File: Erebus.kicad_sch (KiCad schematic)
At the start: 1 part, among them U1 STM32F303CBTx

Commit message: Setup Base Layout
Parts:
- added ENCODER1: EC11E, PCM_marbastlib-various:ROT_Alps_EC11E-Switch, symbol Device:RotaryEncoder_Switch
- added JP1, JP2: Jumper_2_Open, Connector_PinHeader_2.54mm:PinHeader_1x02_P2.54mm_Vertical, symbol Jumper:Jumper_2_Open
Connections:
- net ENCODER_A: now reaches U1.10 (PA0)
- net ENCODER_A: now also ENCODER1.A
- net ENCODER_B: now reaches U1.11 (PA1)
- net ENCODER_B: now also ENCODER1.B
- net GND: now reaches U1.23 (VSS), U1.35 (VSS), U1.47 (VSS)
- net GND: now also U1.8 (VSSA), ENCODER1.C, ENCODER1.S1, JP1.1 (A)
- net ENCODER_SW: now reaches U1.4 (PC15)
- net ENCODER_SW: now also ENCODER1.S2
- new net +3V3: JP2.1 (A)
- new net BOOT0: JP2.2 (B)
- new net ~{RESET}: JP1.2 (B)
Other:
- note added: "Keys"
- note added: "MCU Boot Select Jumpers"
- note added: "Rotary Encoder"
- moved on the sheet: U1

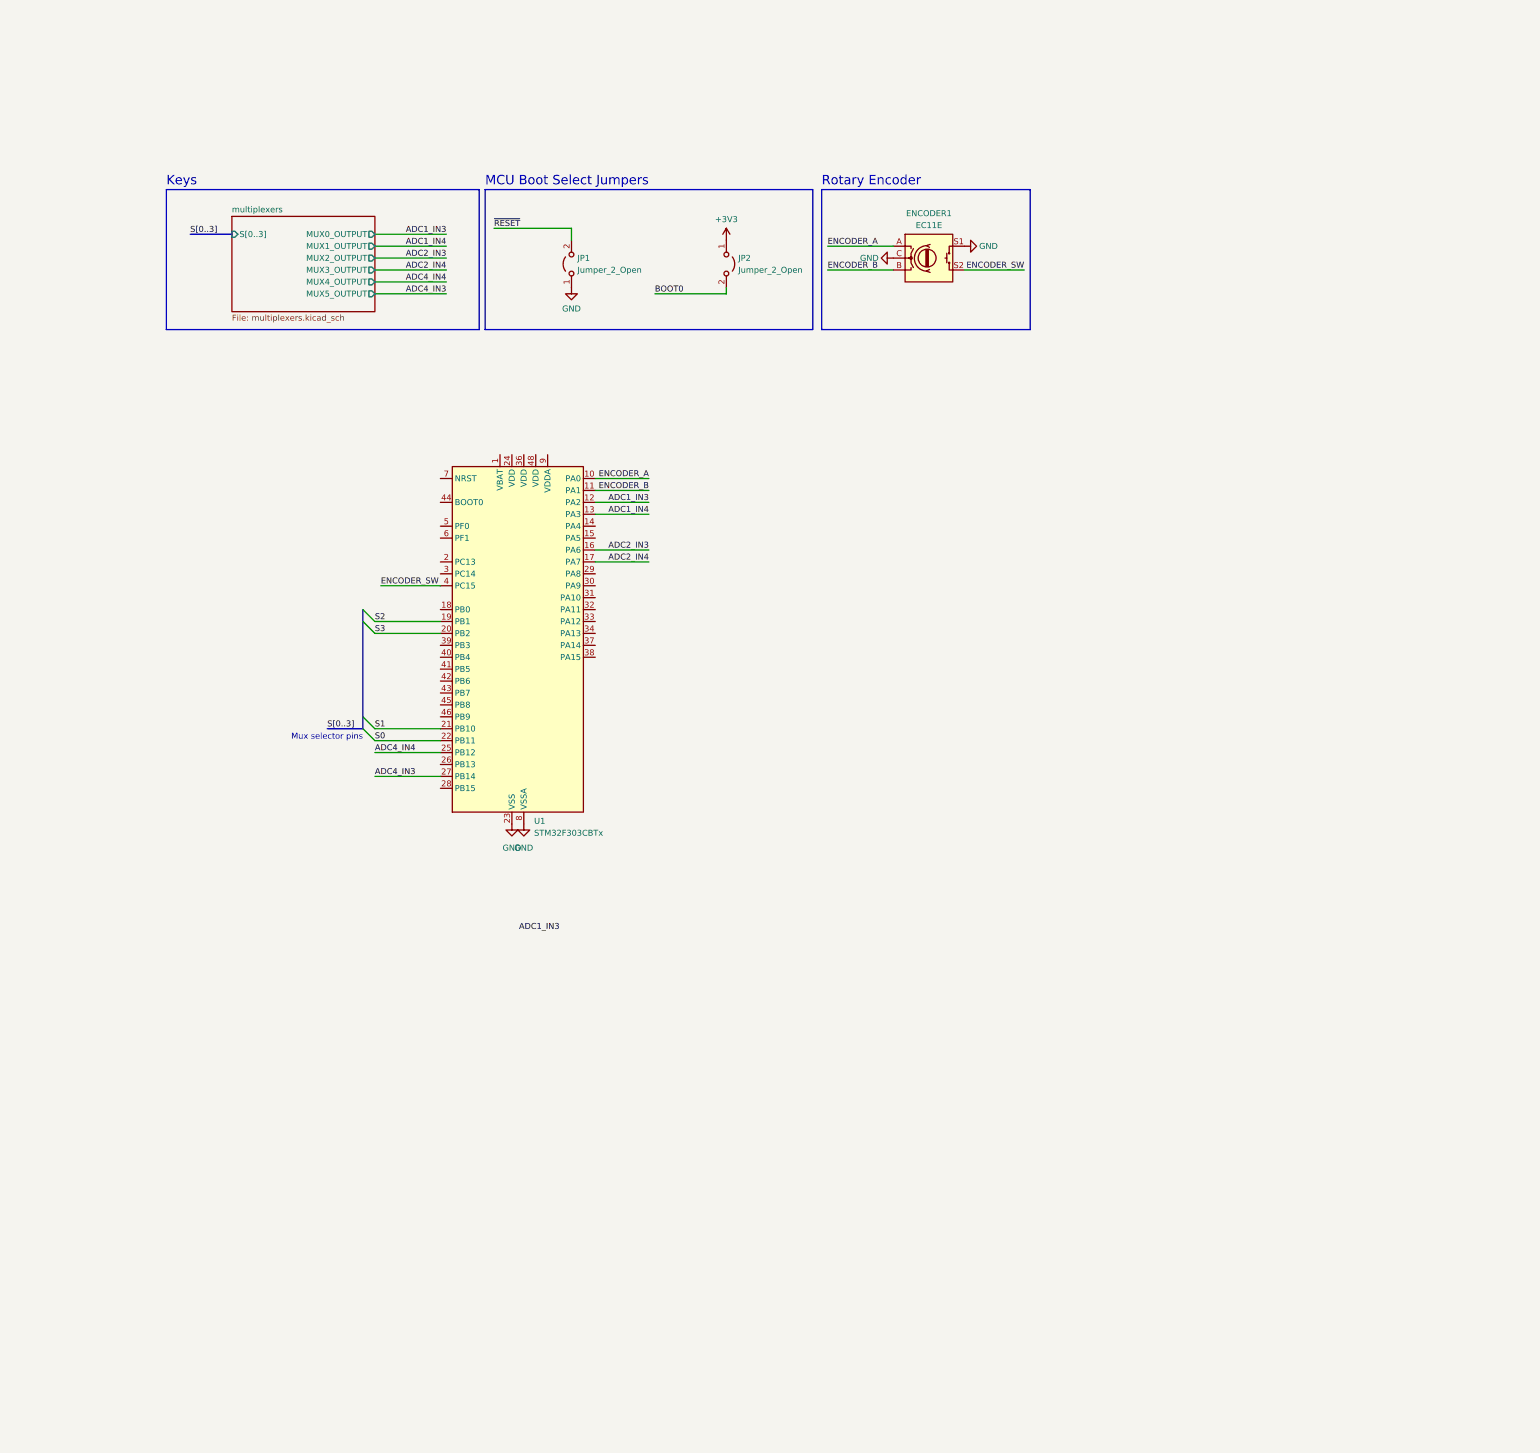
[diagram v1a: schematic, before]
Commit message: Migrating to AT32F415CBT7
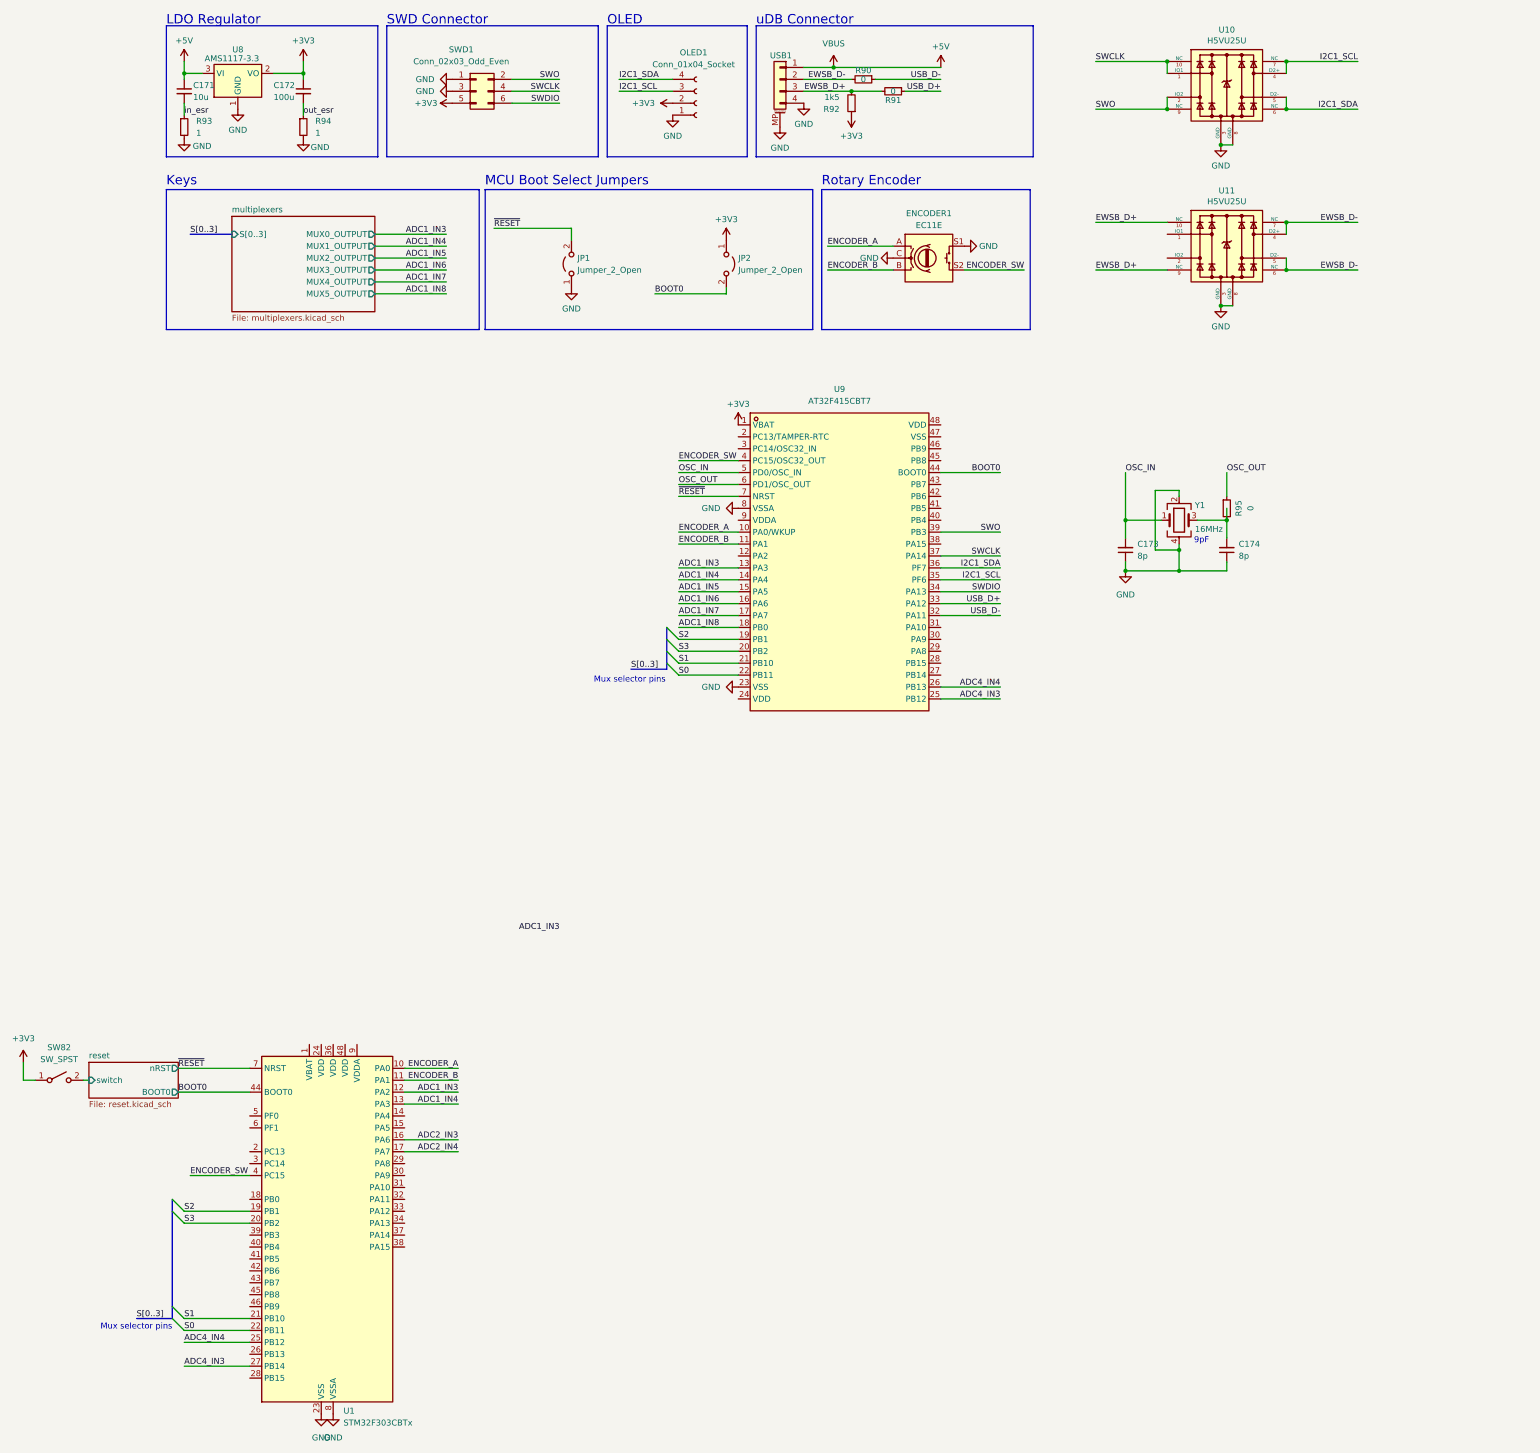
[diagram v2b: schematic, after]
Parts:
- added C171: 10u, Capacitor_SMD:C_1206_3216Metric, symbol Device:C_Small
- added C172: 100u, Capacitor_SMD:C_1206_3216Metric, symbol Device:C_Small
- added C173, C174: 8p, Capacitor_SMD:C_0402_1005Metric, symbol Device:C_Small
- added OLED1: Conn_01x04_Socket, MoonBoard:OLED Module, symbol Connector:Conn_01x04_Socket
- added R90, R91, R95: 0, Resistor_SMD:R_0603_1608Metric_Pad0.98x0.95mm_HandSolder, symbol Device:R_Small
- added R92: 1k5, Resistor_SMD:R_0402_1005Metric, symbol Device:R_Small
- added R93, R94: 1, Resistor_SMD:R_1206_3216Metric, symbol Device:R_Small
- added SW82: SW_SPST, Button_Switch_SMD:SW_SPST_TL3342, symbol Switch:SW_SPST
- added SWD1: Conn_02x03_Odd_Even, Connector_PinHeader_2.54mm:PinHeader_2x03_P2.54mm_Vertical, symbol Connector_Generic:Conn_02x03_Odd_Even
- added U10, U11: H5VU25U, MoonBoard:DFN2510, symbol Unified-Daughterboard-rescue:TPD4E05U06DQAR-acheronSymbols
- added U8: AMS1117-3.3, Package_TO_SOT_SMD:SOT-223-3_TabPin2, symbol Regulator_Linear:AMS1117-3.3
- added U9: AT32F415CBT7, easyeda2kicad:LQFP-48_L7.0-W7.0-P0.50-LS9.0-BL, symbol easyeda2kicad:AT32F415CBT7
- added USB1: X1224WRS-04-LPV01, MoonBoard:PicoEZMate-Reinforced-Alt, symbol Connector_Generic_MountingPin:Conn_01x04_MountingPin
- added Y1: 16MHz, Crystal:Crystal_SMD_3225-4Pin_3.2x2.5mm, symbol Device:Crystal_GND24
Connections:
- net +3V3: now also C172.1, OLED1.2 (Pin_2), R92.1, SW82.1 (A), SWD1.5 (Pin_5), U8.2 (VO), U9.1 (VBAT)
- net ADC1_IN3: now also U9.13 (PA3)
- net ADC1_IN4: now also U9.14 (PA4)
- net ADC4_IN3: now also U9.25 (PB12)
- net ADC4_IN4: now also U9.26 (PB13)
- net BOOT0: now also U1.44 (BOOT0), U9.44 (BOOT0)
- net ENCODER_A: now also U9.10 (PA0/WKUP)
- net ENCODER_B: now also U9.11 (PA1)
- net ENCODER_SW: now also U9.4 (PC15/OSC32_OUT)
- net GND: now also C173.1, C174.1, OLED1.1 (Pin_1), R93.2, R94.2, SWD1.1 (Pin_1), SWD1.3 (Pin_3), U10.3 (GND), U10.8 (GND), U11.3 (GND), U11.8 (GND), U8.1 (GND), U9.23 (VSS), U9.8 (VSSA), USB1.4 (Pin_4), USB1.MP (MountPin), Y1.2, Y1.4
- net S0: now also U9.22 (PB11)
- net S1: now also U9.21 (PB10)
- net S2: now also U9.19 (PB1)
- net S3: now also U9.20 (PB2)
- net ~{RESET}: now also U1.7 (NRST), U9.7 (NRST)
- new net: C174.2, R95.2, Y1.3
- new net +5V: C171.1, U8.3 (VI), USB1.1 (Pin_1)
- new net ADC1_IN5: U9.15 (PA5)
- new net ADC1_IN6: U9.16 (PA6)
- new net ADC1_IN7: U9.17 (PA7)
- new net ADC1_IN8: U9.18 (PB0)
- new net EWSB_D+: R91.2, R92.2, U11.10 (NC), U11.9 (NC), USB1.3 (Pin_3)
- new net EWSB_D-: R90.2, U11.4 (D2+), U11.5 (D2-), U11.6 (NC), U11.7 (NC), USB1.2 (Pin_2)
- new net I2C1_SCL: OLED1.3 (Pin_3), U10.4 (D2+), U10.7 (NC), U9.35 (PF6)
- new net I2C1_SDA: OLED1.4 (Pin_4), U10.5 (D2-), U10.6 (NC), U9.36 (PF7)
- new net OSC_IN: C173.2, U9.5 (PD0/OSC_IN), Y1.1
- new net OSC_OUT: R95.1, U9.6 (PD1/OSC_OUT)
- new net SWCLK: SWD1.4 (Pin_4), U10.1 (IO1), U10.10 (NC), U9.37 (PA14)
- new net SWDIO: SWD1.6 (Pin_6), U9.34 (PA13)
- new net SWO: SWD1.2 (Pin_2), U10.2 (IO2), U10.9 (NC), U9.39 (PB3)
- new net USB_D+: R91.1, U9.33 (PA12)
- new net USB_D-: R90.1, U9.32 (PA11)
- new net in_esr: C171.2, R93.1
- new net out_esr: C172.2, R94.1
- new net reset/switch: SW82.2 (B)
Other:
- added sheet reset (reset.kicad_sch)
- note added: "9pF"
- note added: "LDO Regulator"
- note added: "OLED"
- note added: "SWD Connector"
- note added: "uDB Connector"
- moved on the sheet: U1

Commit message: Routed a lot of the pcb, additionally fixed issues with wrong layout
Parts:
- removed C171: 10u, Capacitor_SMD:C_1206_3216Metric, symbol Device:C_Small
- removed C172: 100u, Capacitor_SMD:C_1206_3216Metric, symbol Device:C_Small
- removed C173, C174: 8p, Capacitor_SMD:C_0402_1005Metric, symbol Device:C_Small
- removed R93, R94: 1, Resistor_SMD:R_1206_3216Metric, symbol Device:R_Small
- removed R95: 0, Resistor_SMD:R_0603_1608Metric_Pad0.98x0.95mm_HandSolder, symbol Device:R_Small
- added C1: 10u, Capacitor_SMD:C_0402_1005Metric, symbol Device:C_Small
- added C2: 100u, Capacitor_SMD:C_0402_1005Metric, symbol Device:C_Small
- added C3, C4: 22p, Capacitor_SMD:C_0402_1005Metric, symbol Device:C_Small
- added H1, H2, H3, H4, H5, H6, H7, H8: MountingHole, MountingHole:MountingHole_2.2mm_M2_Pad, symbol Mechanical:MountingHole
- OLED1: footprint MoonBoard:OLED Module -> Erebus:OLED Module
- U2: renamed from U10; footprint MoonBoard:DFN2510 -> Erebus:DFN2510
- U3: renamed from U11; footprint MoonBoard:DFN2510 -> Erebus:DFN2510
- USB1: footprint MoonBoard:PicoEZMate-Reinforced-Alt -> Erebus:PicoEZMate-Reinforced-Alt
- Y1: value 16MHz -> 8MHz
- renumbered R90 to R1, R91 to R2, R92 to R3, SW82 to SW1, U8 to U1, U9 to U4, U1 to U5
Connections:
- net OSC_OUT is gone; now on net XTAL2: U4.6 (PD1/OSC_OUT)
- net +3V3: now also C2.2
- net +5V: now also C1.2
- net GND: now also C1.1, C2.1, C3.2, C4.2
- net XTAL1: now reaches Y1.3
- net XTAL1: now also U4.5 (PD0/OSC_IN), C3.1
- net OSC_IN renamed XTAL2
- net XTAL2: now also C4.1; no longer U4.5 (PD0/OSC_IN)
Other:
- note removed: "9pF"
- moved on the sheet: U1, Y1
